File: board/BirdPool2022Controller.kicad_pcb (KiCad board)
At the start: 2 copper layers, 26 parts, among them J1 ISP, J2 OSTVN02A150, J3 OSTVN02A150, J4 OSTVN04A150, J5 OSTVN04A150, K1 G5LE-14_DC5, U1 PIC18F1330-I_P, U3 TPC817D_C9G

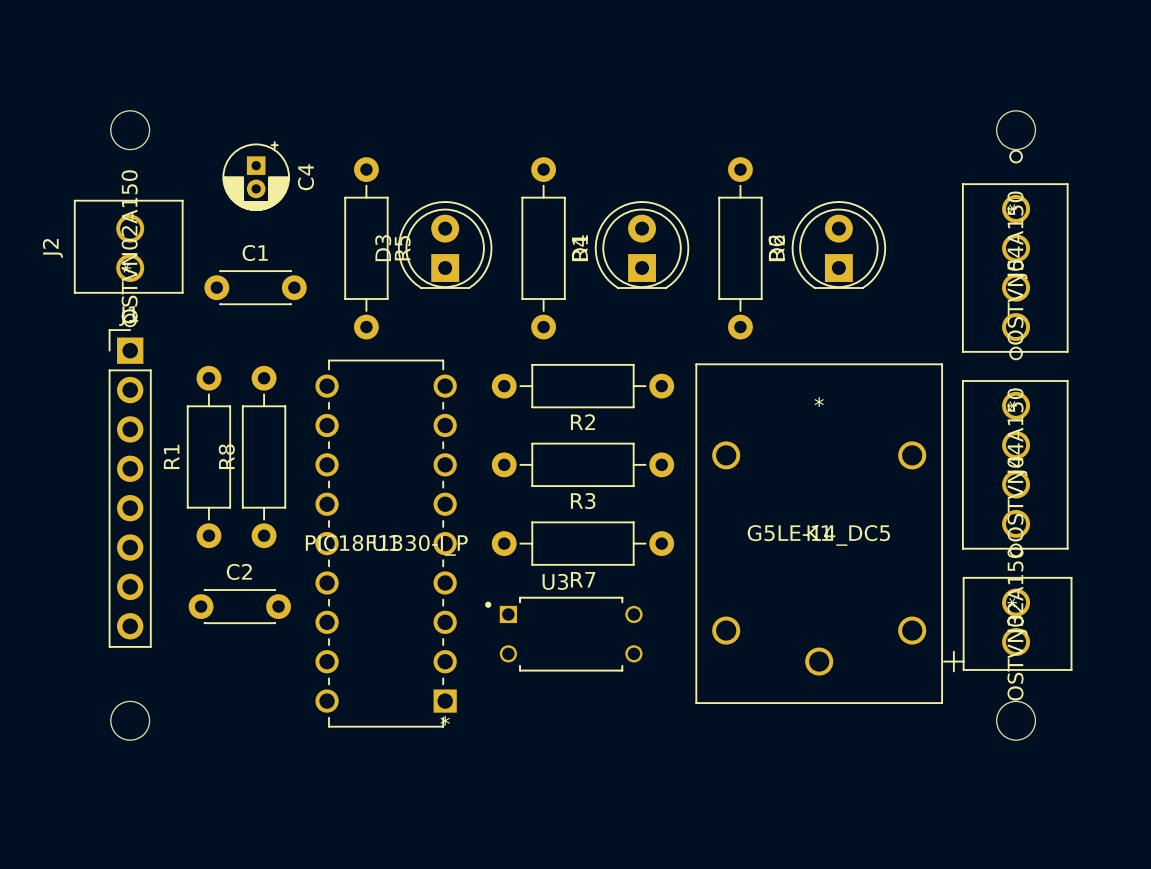
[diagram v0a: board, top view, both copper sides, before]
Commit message: ADD: Board routed
ADD: Board has been routed.
FIX: The relay has been routed with inverted connexion for the coil. This has been fixed.
ADD: 6-pins expansion connector has been added.
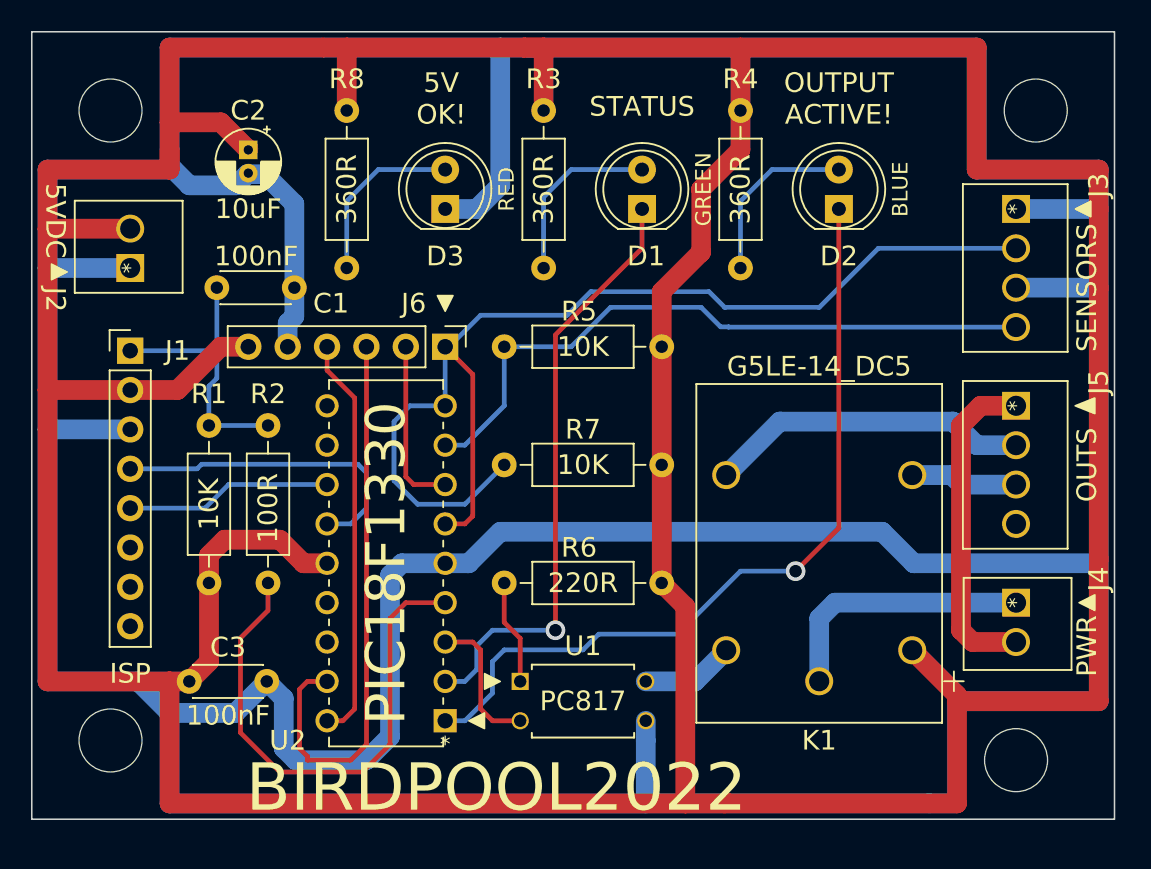
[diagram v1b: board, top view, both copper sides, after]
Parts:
- removed the R5 at (102.9, 64.8)
- removed the U1 at (108.0, 99.1)
- added J6: Conn_01x06, Connector_PinHeader_2.54mm:PinHeader_1x06_P2.54mm_Vertical, F.Cu at (108.0, 76.2)
- added R8: 360R, Resistor_THT:R_Axial_DIN0207_L6.3mm_D2.5mm_P10.16mm_Horizontal, F.Cu at (101.6, 61.0)
- added U2: PIC18F1330, My_Library:PDIP18_300MC_MCH, F.Cu at (108.0, 100.3)
- U1: renamed from U3; value TPC817D_C9G -> PC817
- moved C3 4.89 mm to (91.4, 97.8)
- moved U1 4.38 mm to (116.8, 99.1)
- moved D1 3.81 mm to (120.7, 67.3)
- moved D2 3.81 mm to (133.3, 67.3)
- moved D3 3.81 mm to (108.0, 67.3)
- moved R3 3.81 mm to (114.3, 61.0)
- moved R4 3.81 mm to (127.0, 61.0)
- moved R2 3.06 mm to (96.5, 91.4)
- moved R1 3.05 mm to (92.7, 91.4)
- moved H4 2.54 mm to (144.8, 102.9)
- moved R5 2.54 mm to (121.9, 76.2)
- moved R6 2.54 mm to (121.9, 91.4)
- moved H2 1.80 mm to (146.1, 61.0)
- moved H1 1.80 mm to (86.4, 61.0)
- moved H3 1.80 mm to (86.4, 101.6)
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- renumbered C4 to C2, C2 to C3, J5 to J3, J3 to J4, J4 to J5, R8 to R2, R4 to R3, R6 to R4, R2 to R5, R7 to R6, R3 to R7
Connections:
- K1 pad 2: Net-(K1-Pad2) -> +5V
- K1 pad 5: +5V -> Net-(K1-Pad5)
- U1 pad 4: Net-(K1-Pad2) -> Net-(K1-Pad5)
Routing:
- net GND: track 0.00 -> 368.7 mm
- net +5V: track 0.00 -> 344.0 mm
- net Net-(J3-Pad2): track 0.00 -> 60.3 mm
- net *LED_VALVE_ON: track 0.00 -> 52.3 mm, vias 0 -> 1
- net Net-(J3-Pad4): track 0.00 -> 43.3 mm
- net *LED_STATUS: track 0.00 -> 38.9 mm, vias 0 -> 1
- net Net-(J6-Pad3): track 0.00 -> 36.7 mm
- net Net-(R2-Pad1): track 0.00 -> 33.9 mm
- net Net-(J6-Pad4): track 0.00 -> 26.2 mm
- net Net-(J4-Pad2): track 0.00 -> 21.2 mm
- net Net-(J1-Pad4): track 0.00 -> 20.8 mm
- net Net-(J5-Pad2): track 0.00 -> 20.8 mm
- net Net-(C1-Pad1): track 0.00 -> 18.5 mm
- net Net-(J4-Pad1): track 0.00 -> 17.2 mm
- net Net-(J6-Pad1): track 0.00 -> 13.6 mm
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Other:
- board outline added: 69.8 x 50.8 mm
- net class Default: clearance 0.2 -> 0.3302; trace_width 0.25 -> 0.3048; via_dia 0.8 -> 1.016; via_drill 0.4 -> 0.508
- rule trace_clearance: 0.2 -> 0.3302
- board text added: "5V OK!"
- board text added: "5VDC"
- board text added: "BIRDPOOL2022"
- board text added: "OUTPUT ACTIVE!"
- board text added: "OUTS"
- board text added: "PWR"
- board text added: "SENSORS"
- board text added: "STATUS"

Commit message: FIX: Arrange PCB
ADD: Keepout area around mounting hole.
ADD: Keepout area added around relay related traces.
ADD: Use copper pour for  both ground and power traces.
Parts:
- C2: footprint Capacitor_THT:CP_Radial_D4.0mm_P1.50mm -> Capacitor_THT:CP_Radial_D4.0mm_P2.00mm
- J1: value ISP -> PIC ISP
- moved H4 1.80 mm to (146.1, 101.6)
- moved C2 1.27 mm to (95.2, 64.8)
- moved C3 0.51 mm to (91.9, 97.8)
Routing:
- net GND: track 368.7 -> 34.7 mm
- net +5V: track 344.0 -> 36.1 mm
- net Net-(J6-Pad2): track 11.1 -> 18.4 mm
- net Net-(J6-Pad3): track 36.7 -> 35.4 mm
- net Net-(J1-Pad4): track 20.8 -> 19.6 mm
- net Net-(C1-Pad1): track 18.5 -> 17.6 mm
- net Net-(J4-Pad1): track 17.2 -> 16.3 mm
- added copper zone on F.Cu, net +5V
- added copper zone on B.Cu, net GND
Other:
- board text added: "Rev-0"
